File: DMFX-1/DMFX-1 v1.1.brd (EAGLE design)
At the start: 144 x 100 mm, 568 parts, among them IC2 SN74HC4066D, J1 USB-MINIB-5PIN, J1-2 USB-MINIB-5PIN, J10 MONOSW3C, J11 DM3BT-DSF-PEJS, J2 USB-B-SMT, J3 STEREOSW3C, J4 HEADPHONES, J5 87409-110LF, J6 DM3BT-DSF-PEJS, J7 87409-110LF, J8 DCJ0202, J9 MONOSW3C, Q1 MUN2214T1, Q10 MUN2214T1, Q2 MUN2214T1, Q3 MMBF4393, Q4 MUN2214T1, Q5 2N7002ET1G, Q6 2N7002ET1G, Q7 2N7002ET1G, Q8 MUN2214T1, Q9 MUN2214T1, SW1 MB2011SB1W03-DA, SW2 OS102011MA1Q, U10X 24C64SM, U11X TPS73201DBVT, U12X TPS562209SO, U13 741G3157DBVR, U14 ASDM1-12.000MHZ-LC-T, U15X CDCLVC1108PWR, U17 TLV320AIC3204IRHBT, U18 SN74CBTLV3245APW, U19 LME49721, U1X TPS562209SO, U2 AT93C46A-10TQ-2.7, U20 LME49721, U21 LME49721, U22 LME49721, U23 LME49721, U24 LMV358, U3X TPS3803-01DCKR, U4 TMS320C5535, U5 TMS320C5535, U6 FT2232HL, U7 TPD2E001IDRLRQ1, U8 74LVC1G175DBVSOT95, U9 W25Q64FVSFIG, U9-2 W25Q64FVSFIG, Y1 32.768kHz, Y1-2 32.768kHz

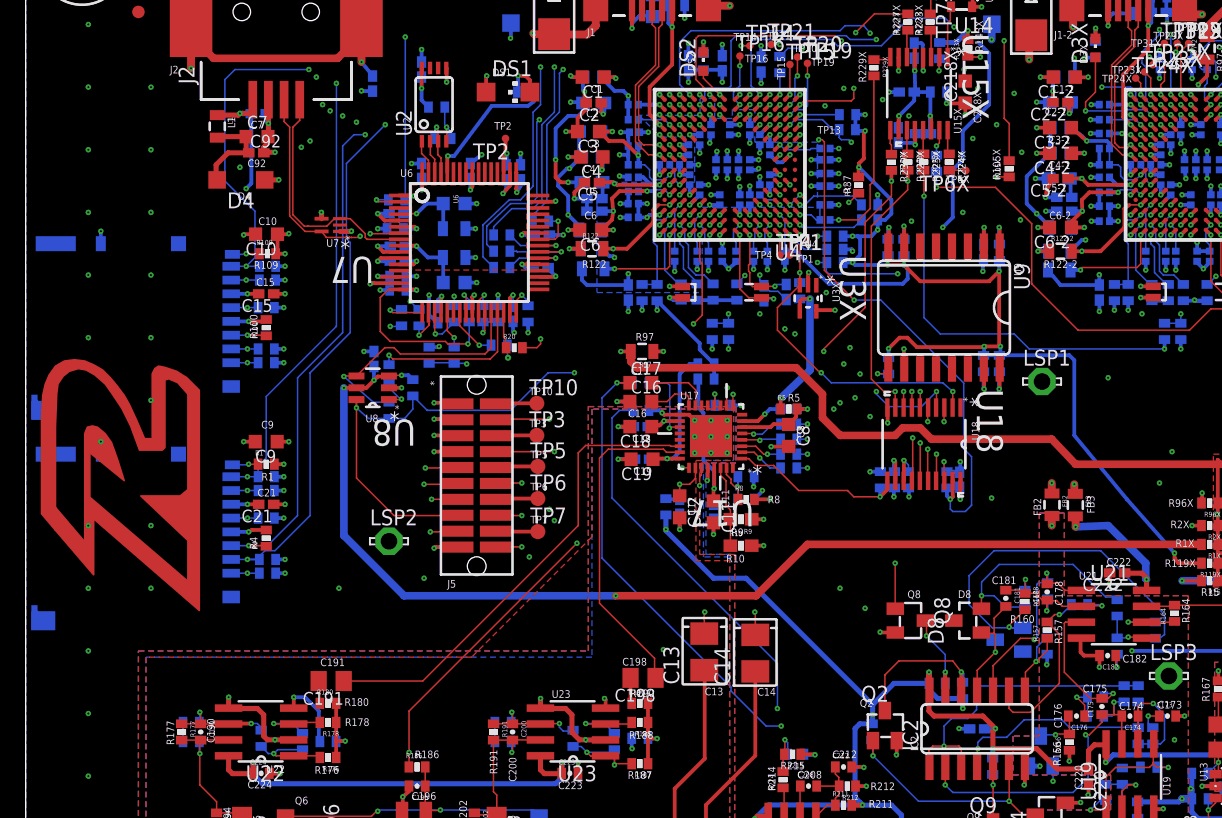
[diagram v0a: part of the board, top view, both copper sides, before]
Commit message: 
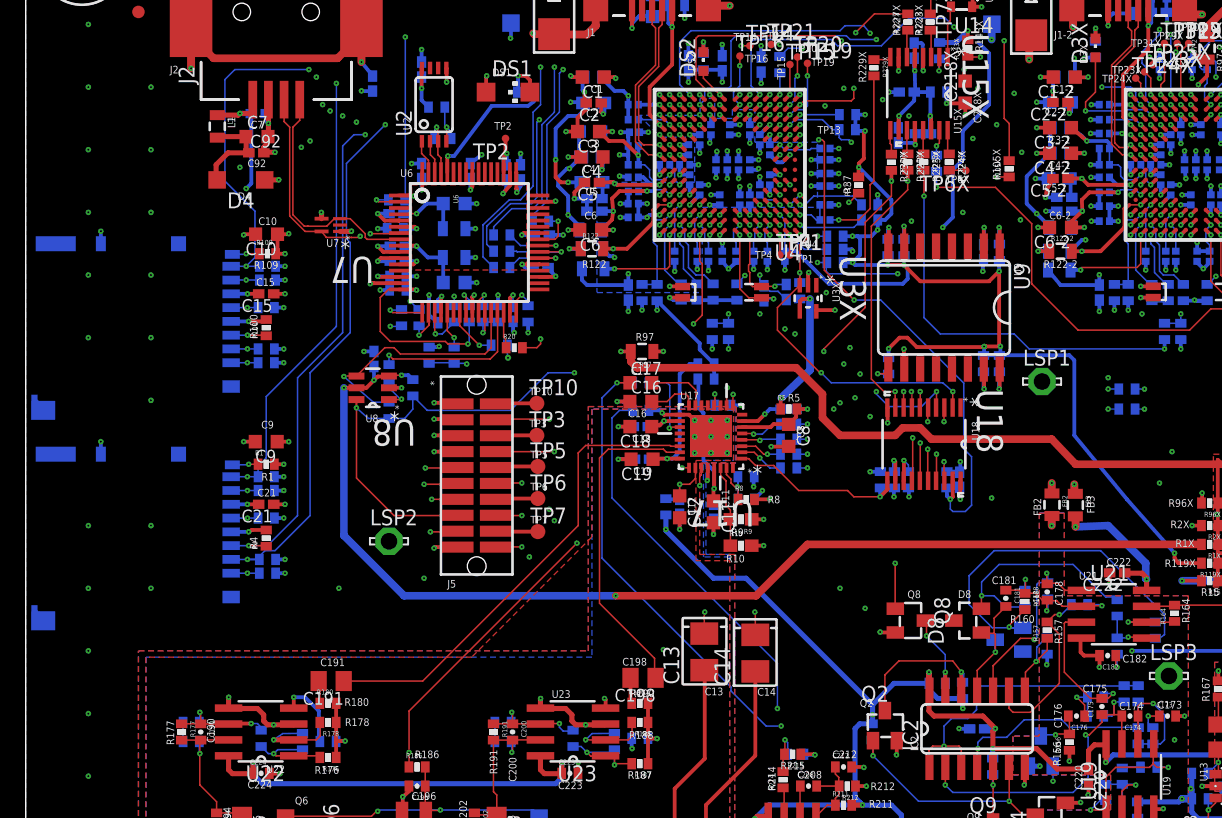
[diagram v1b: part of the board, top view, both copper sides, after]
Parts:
- removed U$172: (no value), rezzonics:REZZLOGO
- added R26, R31: 0, SparkFun:0402-RES
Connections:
- net I2C2_SCL: now also R26.1
- net I2C2_SDA: now also R31.1
- net I2C_SCL: now also R26.2
- net I2C_SDA: now also R31.2
- net N$138: now also U22.2; no longer U22.3
- net N$149: now also U23.2; no longer U23.3
- net V1.65: now also U22.3, U23.3; no longer U22.2, U23.2
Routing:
- net I2C_SDA: track 23.4 -> 41.9 mm, vias 4 -> 5
- net I2C_SCL: track 29.3 -> 46.8 mm, vias 4 -> 5
- net I2C2_SCL: track 20.3 -> 32.3 mm, vias 2 -> 3
- net I2C2_SDA: track 17.3 -> 28.4 mm, vias 2 -> 3
- net V1.65: track 52.5 -> 50.4 mm
- net N$149: track 6.35 -> 7.64 mm
- net N$138: track 6.37 -> 7.40 mm
- net I2S2_RX: track 52.5 -> 53.5 mm
- net GPAIN2: track 81.3 -> 82.0 mm
